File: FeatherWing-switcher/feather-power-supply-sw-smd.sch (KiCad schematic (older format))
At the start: 30 parts, among them J1 5.08mm, J2 Conn_01x12, J3 Conn_01x16, J4 QWIIC, J5 0.1\"x4, Q1 Q_PMOS_GSD, U1 TPS5405DR

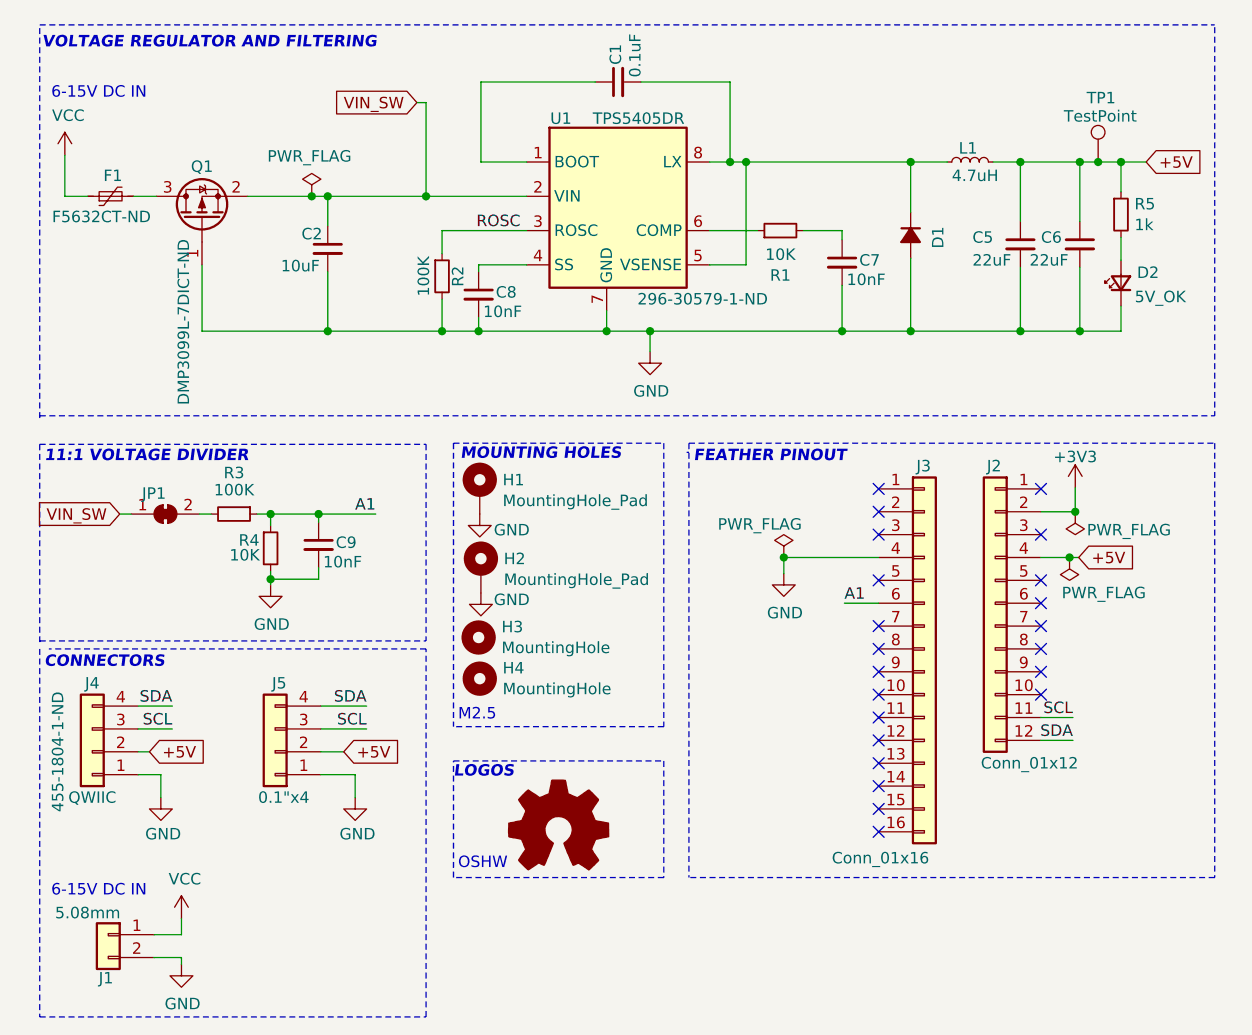
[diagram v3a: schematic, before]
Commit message: clean up schematic and bump to v1.1
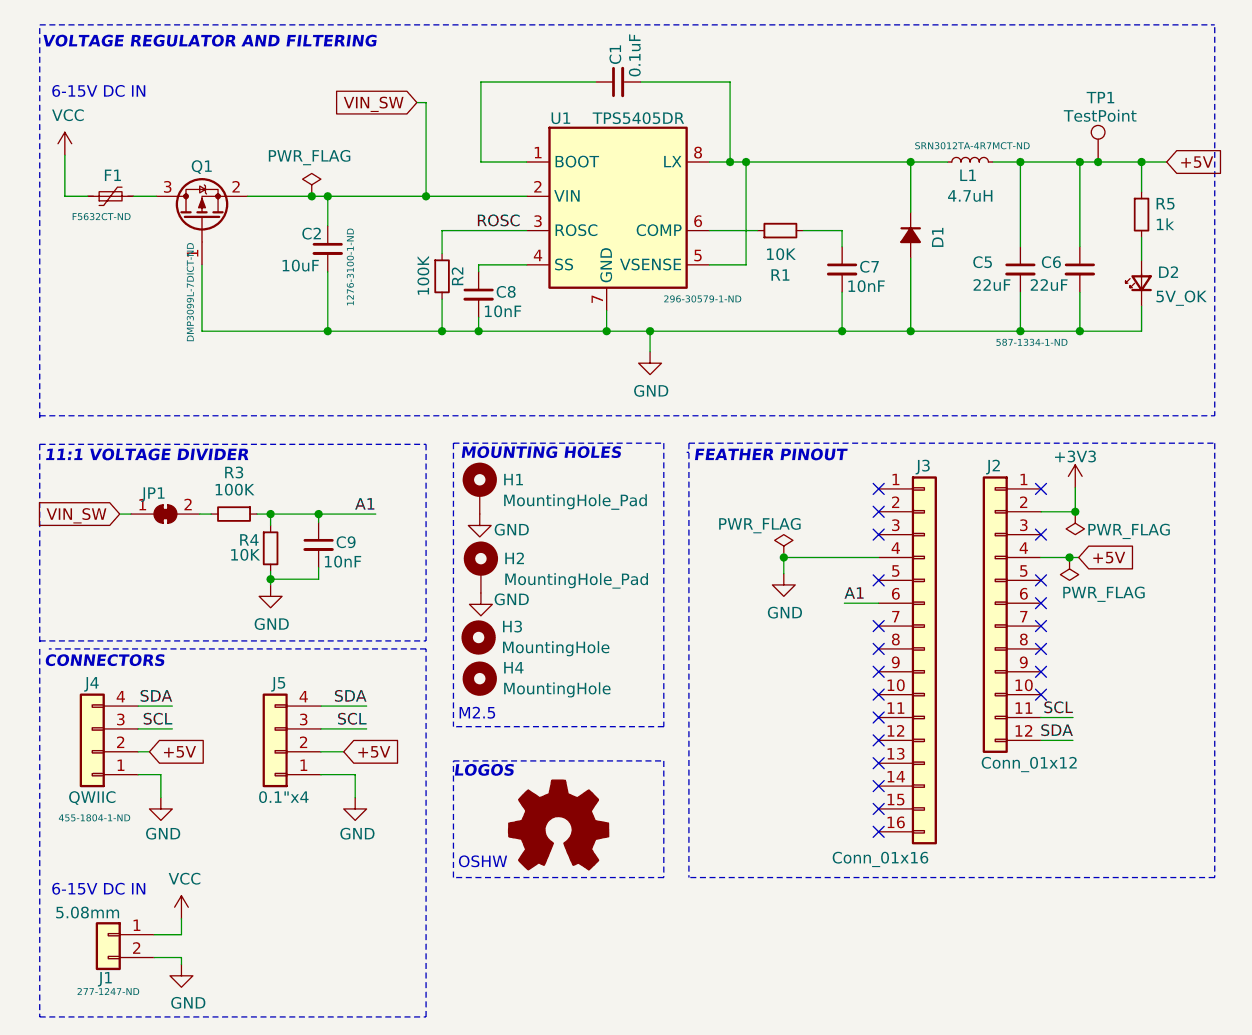
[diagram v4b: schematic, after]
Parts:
- D1: DigiKey-PN (none) -> SMD24PL-TPMSCT-ND; MPN (none) -> SMD24PL-TP
- J1: Digikey_PN (none) -> 277-1247-ND; MPN (none) -> 1729128; Manufacturer (none) -> Phoenix Contact
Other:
- moved on the sheet: C5, C6, C7, D2, R5
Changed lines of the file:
@@
 Title "Feather Switcher"
 Date "2020-09-21"
-Rev "0.1"
+Rev "1.1"
 Comp ""
 Comment1 "Adafruit FeatherWing compatible 5V switching power supply"
-Comment2 ""
-Comment3 ""
-Comment4 ""
+Comment2 "All capacitors are 0603 X7R class unless noted. C2,C5,C6 are 1206, low esr"
+Comment3 "All resistors are 1% 0603"
+Comment4 "Purple text indicate DigiKey part numbers"
 $EndDescr
 $Comp
@@
 NoConn ~ 6740 5100
 $Comp
-L Device:D_Small_ALT D1
-U 1 1 5F43743A
-P 6880 2490
-F 0 "D1" H 6890 2610 50  0000 C CNN
-F 1 "~" H 7000 2580 50  0000 C CNN
-F 2 "Diode_SMD:D_SOD-123F" V 6880 2490 50  0001 C CNN
-F 3 "" V 6880 2490 50  0001 C CNN
-F 4 "" H 6880 2490 50  0001 C CNN "MPN"
-F 5 "" H 6880 2490 50  0001 C CNN "DigiKey-PN"
-	1    6880 2490
-	0    1    1    0
-$EndComp
-Text GLabel 7910 2170 2    50   Input ~ 0
-+5V
-$Comp
 L Device:C_Small C8
 U 1 1 5F4EB59F
@@
 L Device:C_Small C7
 U 1 1 5F4EE168
-P 6580 2610
-F 0 "C7" H 6655 2620 50  0000 L CNN
-F 1 "10nF" H 6600 2535 50  0000 L CNN
-F 2 "Capacitor_SMD:C_0603_1608Metric_Pad1.05x0.95mm_HandSolder" H 6580 2610 50  0001 C CNN
-F 3 "~" H 6580 2610 50  0001 C CNN
-	1    6580 2610
+P 6580 2640
+F 0 "C7" H 6655 2650 50  0000 L CNN
+F 1 "10nF" H 6600 2565 50  0000 L CNN
+F 2 "Capacitor_SMD:C_0603_1608Metric_Pad1.05x0.95mm_HandSolder" H 6580 2640 50  0001 C CNN
+F 3 "~" H 6580 2640 50  0001 C CNN
+	1    6580 2640
 	1    0    0    -1
 $EndComp
@@
 F 2 "Capacitor_SMD:C_1206_3216Metric_Pad1.42x1.75mm_HandSolder" H 4330 2550 50  0001 C CNN
 F 3 "~" H 4330 2550 50  0001 C CNN
-F 4 "1276-3100-1-ND‎" H 4330 2550 50  0001 C CNN "DigiKey_PN"
+F 4 "1276-3100-1-ND‎" V 4430 2470 30  0000 C CNN "DigiKey_PN"
 	1    4330 2550
 	1    0    0    -1
@@
 	7240 2170 7360 2170
 Wire Wire Line
-	7360 2170 7360 2430
+	7360 2170 7360 2540
 Wire Wire Line
 	7360 2170 7620 2170
@@
 	6410 2470 6580 2470
 Wire Wire Line
-	6580 2470 6580 2510
-Wire Wire Line
-	6580 2710 6580 2910
+	6580 2470 6580 2540
+Wire Wire Line
+	6580 2740 6580 2910
 Wire Wire Line
 	6880 2590 6880 2910
 Wire Wire Line
-	7360 2630 7360 2910
+	7360 2740 7360 2910
 Wire Wire Line
 	5200 2170 5000 2170
@@
 F 3 "https://www.ti.com/lit/ds/symlink/tps5405.pdf" H 5600 2320 50  0001 C CNN
 F 4 "TPS5405DR" H 5600 2320 50  0001 C CNN "MPN"
-F 5 "296-30579-1-ND" H 5970 1870 50  0000 C CNN "Digikey_PN"
+F 5 "296-30579-1-ND" H 5970 1870 30  0000 C CNN "Digikey_PN"
 	1    5600 2320
 	1    0    0    -1
@@
 U 1 1 5F4D1082
 P 7140 2170
-F 0 "L1" V 7200 2220 50  0000 R CNN
-F 1 "4.7uH" V 7080 2250 50  0000 R CNN
+F 0 "L1" V 7080 2220 50  0000 R CNN
+F 1 "4.7uH" V 6990 2270 50  0000 R CNN
 F 2 "My libs:TDK-VLS4012HBX" H 7140 2170 50  0001 C CNN
 F 3 "~" H 7140 2170 50  0001 C CNN
-F 4 "SRN3012TA-4R7MCT-ND‎" V 7140 2170 50  0001 C CNN "DigiKey_PN"
+F 4 "SRN3012TA-4R7MCT-ND‎" V 7210 2160 30  0000 C CNN "DigiKey_PN"
 	1    7140 2170
 	0    -1   -1   0
 $EndComp
-$Comp
-L Device:C_Small C6
-U 1 1 5F5C3C5E
-P 7620 2530
-F 0 "C6" H 7450 2560 50  0000 L CNN
-F 1 "22uF" H 7400 2460 50  0000 L CNN
-F 2 "Capacitor_SMD:C_1210_3225Metric_Pad1.42x2.65mm_HandSolder" H 7620 2530 50  0001 C CNN
-F 3 "https://www.yuden.co.jp/productdata/catalog/mlcc06_e.pdf" H 7620 2530 50  0001 C CNN
-F 4 "587-1334-1-ND" H 7620 2530 50  0001 C CNN "DigiKey_PN"
-	1    7620 2530
-	1    0    0    -1
-$EndComp
-Wire Wire Line
-	7620 2430 7620 2170
+Wire Wire Line
+	7620 2540 7620 2170
 Connection ~ 7620 2170
 Wire Wire Line
 	7620 2170 7700 2170
 Wire Wire Line
-	7620 2630 7620 2910
+	7620 2740 7620 2910
 Wire Wire Line
 	6880 2910 7360 2910
@@
 	1    0    0    -1
 $EndComp
-$Comp
-L Device:C_Small C5
-U 1 1 5F4359CD
-P 7360 2530
-F 0 "C5" H 7150 2560 50  0000 L CNN
-F 1 "22uF" H 7150 2460 50  0000 L CNN
-F 2 "Capacitor_SMD:C_1210_3225Metric_Pad1.42x2.65mm_HandSolder" H 7360 2530 50  0001 C CNN
-F 3 "https://www.yuden.co.jp/productdata/catalog/mlcc06_e.pdf" H 7360 2530 50  0001 C CNN
-F 4 "587-1334-1-ND" H 7360 2530 50  0001 C CNN "DigiKey_PN"
-	1    7360 2530
-	1    0    0    -1
-$EndComp
 Wire Wire Line
 	3770 3710 3820 3710
@@
 F 2 "Connector_JST:JST_SH_SM04B-SRSS-TB_1x04-1MP_P1.00mm_Horizontal" H 3300 4750 50  0001 C CNN
 F 3 "https://cdn-shop.adafruit.com/product-files/4328/4328_C13916-001_CCSH-W10-04-BK-RC-A.pdf" H 3300 4750 50  0001 C CNN
-F 4 "455-1804-1-ND" V 3450 4750 50  0000 C CNN "DigiKey_PN"
+F 4 "455-1804-1-ND" H 3290 5040 30  0000 C CNN "DigiKey_PN"
 	1    3300 4750
 	-1   0    0    1
@@
 F 2 "Fuse:Fuse_1812_4532Metric_Castellated" H 3430 2120 50  0001 L CNN
 F 3 "~" H 3380 2320 50  0001 C CNN
-F 4 "F5632CT-ND" V 3290 2360 50  0000 C CNN "DigiKey-PN"
+F 4 "F5632CT-ND" V 3290 2360 30  0000 C CNN "DigiKey-PN"
 F 5 "1812L110/24DR" V 3380 2320 50  0001 C CNN "MPN"
 F 6 "Littelfuse Inc." V 3380 2320 50  0001 C CNN "LittleFuse"
@@
 Wire Wire Line
 	4300 4750 4400 4750
-$Comp
-L Device:LED_Small D2
-U 1 1 5F672EB4
-P 7800 2700
-F 0 "D2" V 7846 2630 50  0000 R CNN
-F 1 "5V_OK" V 7740 2640 50  0000 R CNN
-F 2 "LED_SMD:LED_0805_2012Metric_Castellated" V 7800 2700 50  0001 C CNN
-F 3 "~" V 7800 2700 50  0001 C CNN
-	1    7800 2700
-	0    -1   -1   0
-$EndComp
-$Comp
-L Device:R_Small R5
-U 1 1 5F673EBF
-P 7800 2400
-F 0 "R5" H 7859 2446 50  0000 L CNN
-F 1 "1k" H 7859 2355 50  0000 L CNN
-F 2 "Resistor_SMD:R_0603_1608Metric_Pad1.05x0.95mm_HandSolder" H 7800 2400 50  0001 C CNN
-F 3 "~" H 7800 2400 50  0001 C CNN
-	1    7800 2400
-	1    0    0    -1
-$EndComp
-Wire Wire Line
-	7800 2170 7800 2300
-Connection ~ 7800 2170
-Wire Wire Line
-	7800 2170 7910 2170
-Wire Wire Line
-	7800 2500 7800 2600
-Wire Wire Line
-	7800 2800 7800 2910
-Wire Wire Line
-	7800 2910 7620 2910
-Connection ~ 7620 2910
 Wire Notes Line
 	3070 1570 8210 1570
@@
 F 3 "https://www.diodes.com/assets/Datasheets/DMP3099L.pdf" H 3780 2420 50  0001 C CNN
 F 4 "DMP3099L-7" V 3780 2420 50  0001 C CNN "MPN"
-F 5 "DMP3099L-7DICT-ND" H 3330 2500 50  0000 C CNN "Digikey_PN"
+F 5 "DMP3099L-7DICT-ND" H 3460 2470 30  0000 C CNN "Digikey_PN"
 	1    3780 2420
 	0    -1   -1   0
@@
 P 3690 5680
 F 0 "#PWR011" H 3690 5430 50  0001 C CNN
-F 1 "GND" H 3695 5507 50  0000 C CNN
+F 1 "GND" H 3720 5510 50  0000 C CNN
 F 2 "" H 3690 5680 50  0001 C CNN
 F 3 "" H 3690 5680 50  0001 C CNN
@@
 	1    0    0    -1
 $EndComp
-Connection ~ 7700 2170
-Wire Wire Line
-	7700 2170 7800 2170
 Text Notes 4900 4620 0    50   ~ 0
 M2.5
@@
 F 2 "TerminalBlock_Phoenix:TerminalBlock_Phoenix_MKDS-1,5-2_1x02_P5.00mm_Horizontal" H 3370 5550 50  0001 C CNN
 F 3 "~" H 3370 5550 50  0001 C CNN
+F 4 "1729128" H 3370 5550 50  0001 C CNN "MPN"
+F 5 "277-1247-ND " H 3370 5300 30  0000 C CNN "Digikey_PN"
+F 6 "Phoenix Contact" H 3370 5550 50  0001 C CNN "Manufacturer"
 	1    3370 5550
 	-1   0    0    -1
@@
 Wire Notes Line
 	4760 4300 3110 4300
+$Comp
+L Device:D_Small_ALT D1
+U 1 1 5F43743A
+P 6880 2490
+F 0 "D1" H 6890 2610 50  0000 C CNN
+F 1 "~" H 7000 2580 50  0000 C CNN
+F 2 "Diode_SMD:D_SOD-123F" V 6880 2490 50  0001 C CNN
+F 3 "https://www.mccsemi.com/pdf/Products/SMD22PL-SMD210PL(SOD-123FL).pdf" V 6880 2490 50  0001 C CNN
+F 4 "SMD24PL-TP" H 6880 2490 50  0001 C CNN "MPN"
+F 5 "SMD24PL-TPMSCT-ND" H 6880 2490 50  0001 C CNN "DigiKey-PN"
+	1    6880 2490
+	0    1    1    0
+$EndComp
+$Comp
+L Device:C_Small C6
+U 1 1 5F5C3C5E
+P 7620 2640
+F 0 "C6" H 7450 2670 50  0000 L CNN
+F 1 "22uF" H 7400 2570 50  0000 L CNN
+F 2 "Capacitor_SMD:C_1210_3225Metric_Pad1.42x2.65mm_HandSolder" H 7620 2640 50  0001 C CNN
+F 3 "https://www.yuden.co.jp/productdata/catalog/mlcc06_e.pdf" H 7620 2640 50  0001 C CNN
+F 4 "587-1334-1-ND" H 7620 2640 50  0001 C CNN "DigiKey_PN"
+	1    7620 2640
+	1    0    0    -1
+$EndComp
+Text GLabel 8000 2170 2    50   Input ~ 0
++5V
+$Comp
+L Device:LED_Small D2
+U 1 1 5F672EB4
+P 7890 2700
+F 0 "D2" V 7936 2630 50  0000 R CNN
+F 1 "5V_OK" V 7830 2640 50  0000 R CNN
+F 2 "LED_SMD:LED_0805_2012Metric_Castellated" V 7890 2700 50  0001 C CNN
+F 3 "~" V 7890 2700 50  0001 C CNN
+	1    7890 2700
+	0    -1   -1   0
+$EndComp
+$Comp
+L Device:R_Small R5
+U 1 1 5F673EBF
+P 7890 2400
+F 0 "R5" H 7949 2446 50  0000 L CNN
+F 1 "1k" H 7949 2355 50  0000 L CNN
+F 2 "Resistor_SMD:R_0603_1608Metric_Pad1.05x0.95mm_HandSolder" H 7890 2400 50  0001 C CNN
+F 3 "~" H 7890 2400 50  0001 C CNN
+	1    7890 2400
+	1    0    0    -1
+$EndComp
+Wire Wire Line
+	7890 2170 7890 2300
+Connection ~ 7890 2170
+Wire Wire Line
+	7890 2170 8000 2170
+Wire Wire Line
+	7890 2500 7890 2600
+Wire Wire Line
+	7890 2800 7890 2910
+Wire Wire Line
+	7700 2170 7890 2170
+Connection ~ 7700 2170
+Wire Wire Line
+	7890 2910 7620 2910
+Connection ~ 7620 2910
+$Comp
+L Device:C_Small C5
+U 1 1 5F4359CD
+P 7360 2640
+F 0 "C5" H 7150 2670 50  0000 L CNN
+F 1 "22uF" H 7150 2570 50  0000 L CNN
+F 2 "Capacitor_SMD:C_1210_3225Metric_Pad1.42x2.65mm_HandSolder" H 7360 2640 50  0001 C CNN
+F 3 "https://www.yuden.co.jp/productdata/catalog/mlcc06_e.pdf" H 7360 2640 50  0001 C CNN
+F 4 "587-1334-1-ND" H 7410 2320 30  0000 C CNN "DigiKey_PN"
+	1    7360 2640
+	1    0    0    -1
+$EndComp
 $EndSCHEMATC

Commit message: v1.0 schematic cleanup
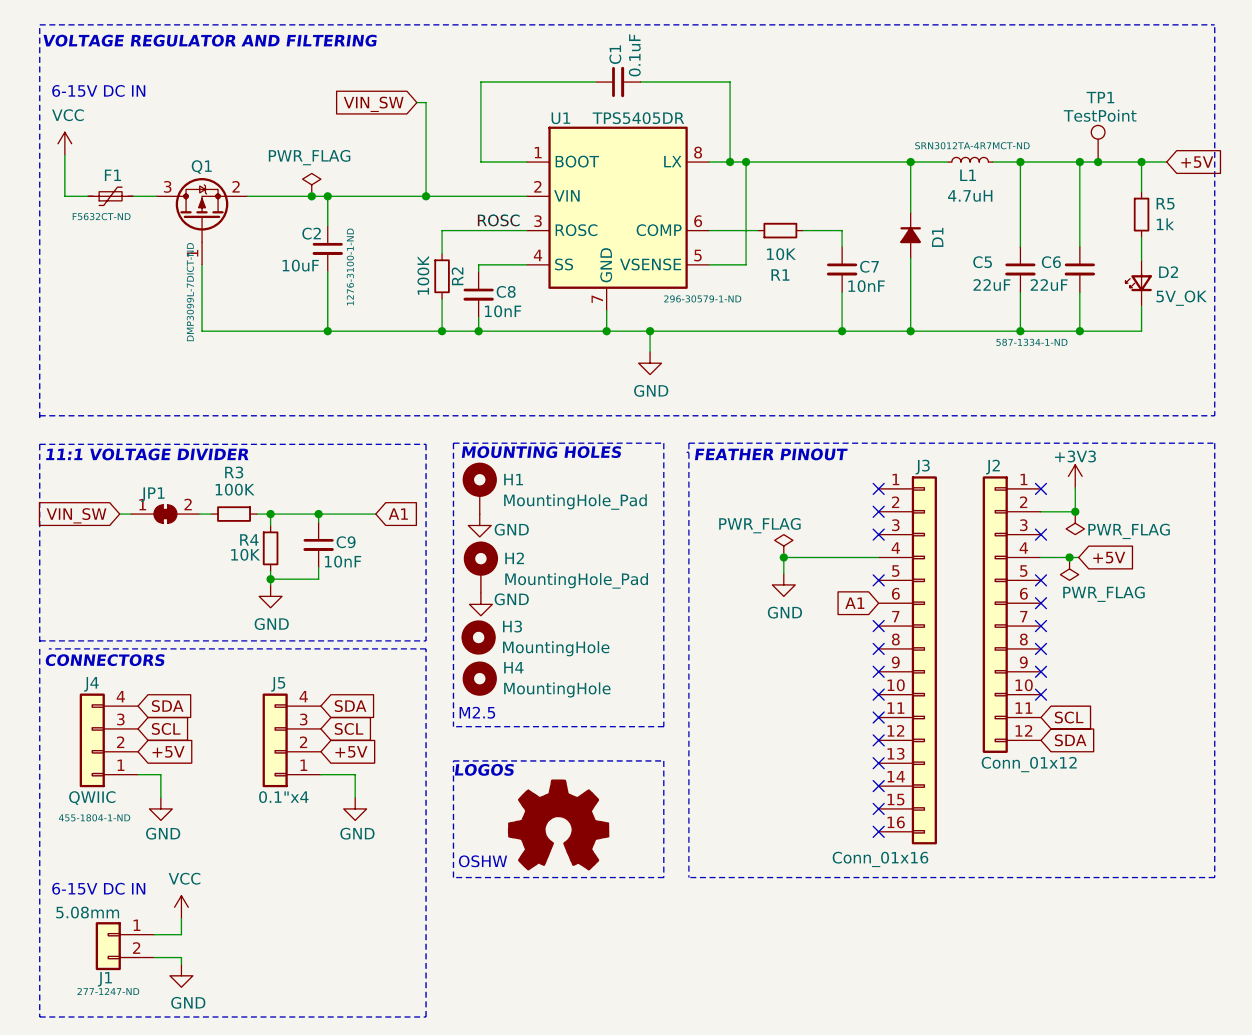
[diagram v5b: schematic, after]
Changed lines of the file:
@@
 $EndComp
 Connection ~ 6325 3900
-Wire Wire Line
-	6590 4100 6740 4100
 NoConn ~ 7450 3800
 NoConn ~ 7450 4000
@@
 Wire Wire Line
 	4290 3745 4290 3710
-Connection ~ 4290 3710
 Wire Wire Line
 	4290 3710 4080 3710
@@
 $EndComp
 Connection ~ 7600 3700
-Text Label 4540 3710 2    50   ~ 0
-A1
-Text Label 6590 4100 0    50   ~ 0
-A1
-Wire Wire Line
-	7450 4700 7590 4700
-Text Label 7590 4700 2    50   ~ 0
-SDA
-Wire Wire Line
-	3500 4550 3650 4550
-Wire Wire Line
-	3500 4650 3650 4650
-Text Label 3650 4550 2    50   ~ 0
-SDA
-Text Label 3650 4650 2    50   ~ 0
-SCL
-Text GLabel 3550 4750 2    50   Input ~ 0
+Text GLabel 3500 4750 2    50   Input ~ 0
 +5V
-Wire Wire Line
-	3500 4750 3550 4750
 Text Notes 3090 4390 0    50   Italic 10
 CONNECTORS
@@
 	-1   0    0    1
 $EndComp
-Text Label 4500 4650 2    50   ~ 0
-SCL
-Wire Wire Line
-	4300 4550 4500 4550
-Wire Wire Line
-	4300 4650 4500 4650
-Text GLabel 4400 4750 2    50   Input ~ 0
+Text GLabel 4300 4750 2    50   Input ~ 0
 +5V
 $Comp
@@
 Wire Wire Line
 	4450 4850 4450 4950
-Wire Wire Line
-	4300 4750 4400 4750
 Wire Notes Line
 	3070 1570 8210 1570
@@
 Wire Wire Line
 	3600 4850 3500 4850
-Wire Wire Line
-	7450 4600 7590 4600
-Text Label 7590 4600 2    50   ~ 0
-SCL
 $Comp
 L Connector_Generic:Conn_01x16 J3
@@
 	1    0    0    -1
 $EndComp
-Text Label 4500 4550 2    50   ~ 0
-SDA
 $Comp
 L power:VCC #PWR09
@@
 	1    0    0    -1
 $EndComp
+Text GLabel 7450 4600 2    50   Input ~ 0
+SCL
+Text GLabel 7450 4700 2    50   Input ~ 0
+SDA
+Text GLabel 4300 4650 2    50   Input ~ 0
+SCL
+Text GLabel 4300 4550 2    50   Input ~ 0
+SDA
+Text GLabel 3500 4650 2    50   Input ~ 0
+SCL
+Text GLabel 3500 4550 2    50   Input ~ 0
+SDA
+Text GLabel 4540 3710 2    50   Input ~ 0
+A1
+Connection ~ 4290 3710
+Text GLabel 6740 4100 0    50   Input ~ 0
+A1
 $EndSCHEMATC

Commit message: update board to version 2
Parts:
- removed TP1: TestPoint, TestPoint:TestPoint_Pad_D1.5mm, symbol Connector:TestPoint
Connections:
- net GND: now also J1.1 (Pin_1); no longer J1.2 (Pin_2)
- net VCC: now also J1.2 (Pin_2); no longer J1.1 (Pin_1)
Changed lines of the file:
@@
 Sheet 1 1
 Title "Feather Switcher"
-Date "2020-09-21"
-Rev "1.1"
+Date "2020-10-05"
+Rev "2.0"
 Comp ""
 Comment1 "Adafruit FeatherWing compatible 5V switching power supply"
@@
 Connection ~ 7620 2170
 Wire Wire Line
-	7620 2170 7700 2170
-Wire Wire Line
 	7620 2740 7620 2910
 Wire Wire Line
@@
 Wire Wire Line
 	3690 5650 3570 5650
-$Comp
-L Connector:TestPoint TP1
-U 1 1 5F70232D
-P 7700 2170
-F 0 "TP1" H 7650 2450 50  0000 L CNN
-F 1 "TestPoint" H 7550 2370 50  0000 L CNN
-F 2 "TestPoint:TestPoint_Pad_D1.5mm" H 7900 2170 50  0001 C CNN
-F 3 "~" H 7900 2170 50  0001 C CNN
-	1    7700 2170
-	1    0    0    -1
-$EndComp
 Text Notes 4900 4620 0    50   ~ 0
 M2.5
@@
 Wire Wire Line
 	4330 2910 4830 2910
-$Comp
-L Connector_Generic:Conn_01x02 J1
-U 1 1 5F4365A9
-P 3370 5550
-F 0 "J1" H 3380 5360 50  0000 C CNN
-F 1 "5.08mm" H 3460 5645 50  0000 C CNN
-F 2 "TerminalBlock_Phoenix:TerminalBlock_Phoenix_MKDS-1,5-2_1x02_P5.00mm_Horizontal" H 3370 5550 50  0001 C CNN
-F 3 "~" H 3370 5550 50  0001 C CNN
-F 4 "1729128" H 3370 5550 50  0001 C CNN "MPN"
-F 5 "277-1247-ND " H 3370 5300 30  0000 C CNN "Digikey_PN"
-F 6 "Phoenix Contact" H 3370 5550 50  0001 C CNN "Manufacturer"
-	1    3370 5550
-	-1   0    0    -1
-$EndComp
 Text GLabel 4720 1910 0    50   Input ~ 0
 VIN_SW
@@
 Wire Wire Line
 	7890 2800 7890 2910
-Wire Wire Line
-	7700 2170 7890 2170
-Connection ~ 7700 2170
 Wire Wire Line
 	7890 2910 7620 2910
@@
 Text GLabel 6740 4100 0    50   Input ~ 0
 A1
+$Comp
+L Connector_Generic:Conn_01x02 J1
+U 1 1 5F4365A9
+P 3370 5650
+F 0 "J1" H 3380 5460 50  0000 C CNN
+F 1 "5.08mm" H 3460 5745 50  0000 C CNN
+F 2 "TerminalBlock_Phoenix:TerminalBlock_Phoenix_MKDS-1,5-2_1x02_P5.00mm_Horizontal" H 3370 5650 50  0001 C CNN
+F 3 "~" H 3370 5650 50  0001 C CNN
+F 4 "1729128" H 3370 5650 50  0001 C CNN "MPN"
+F 5 "277-1247-ND " H 3440 5810 30  0000 C CNN "Digikey_PN"
+F 6 "Phoenix Contact" H 3370 5650 50  0001 C CNN "Manufacturer"
+	1    3370 5650
+	-1   0    0    1
+$EndComp
+Wire Wire Line
+	7620 2170 7890 2170
 $EndSCHEMATC
